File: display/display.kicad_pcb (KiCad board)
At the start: 2 copper layers, 70 x 30 mm, 4 parts, among them J2 Conn_02x05_Odd_Even, U1 D148K, U2 D148K, U3 D148K

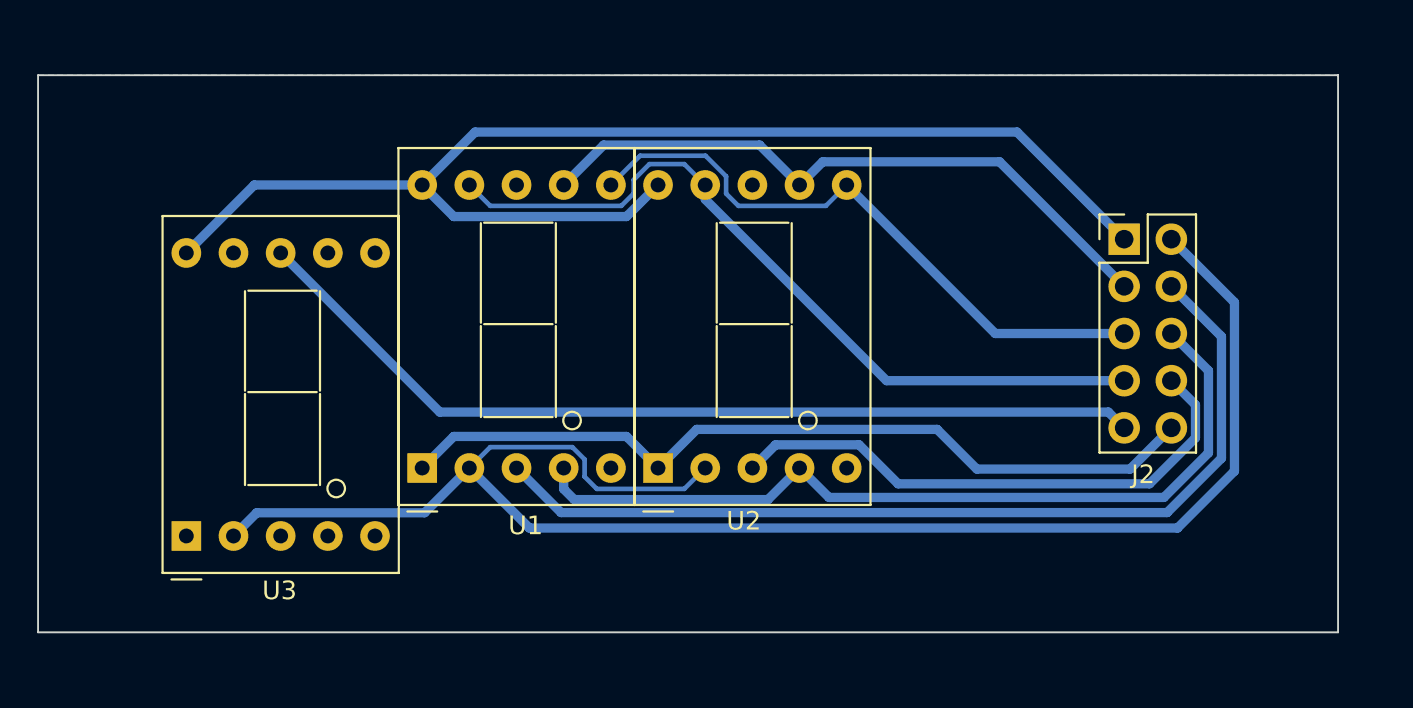
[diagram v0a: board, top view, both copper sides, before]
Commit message: display mod + plano
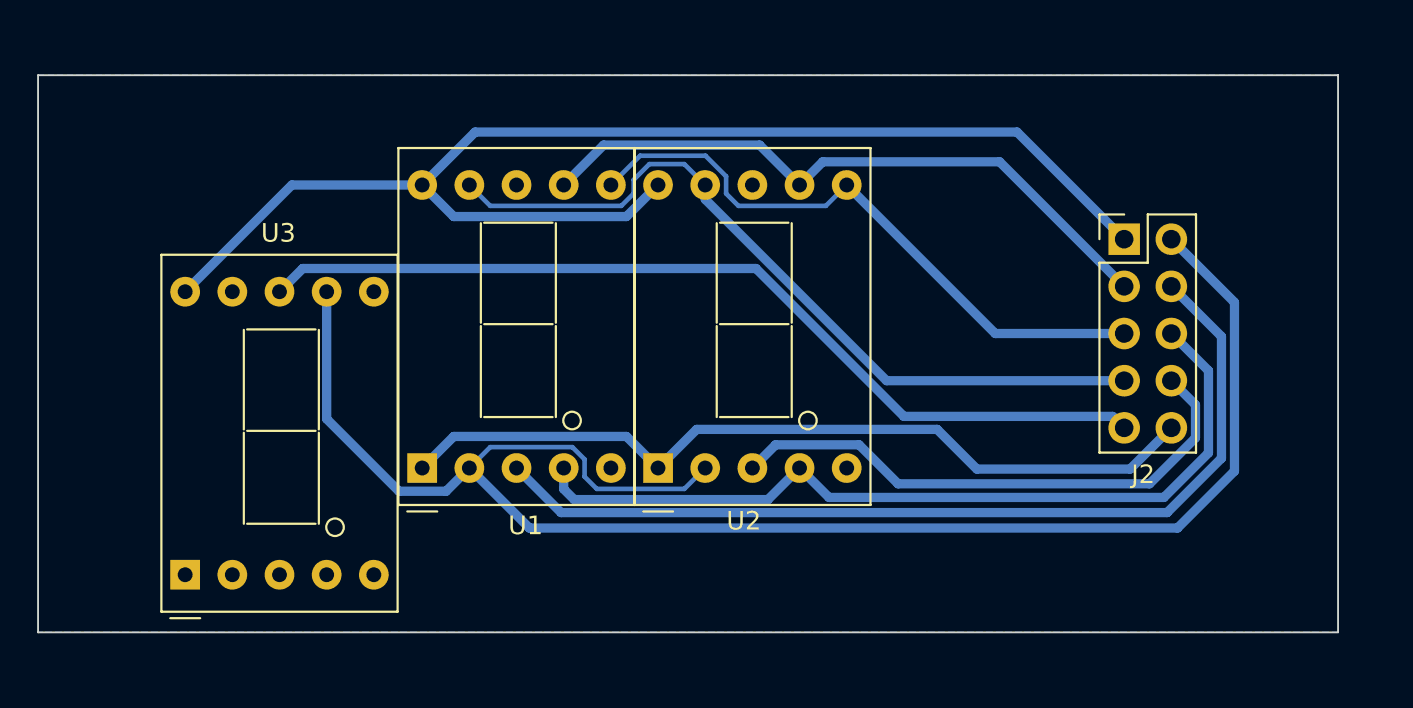
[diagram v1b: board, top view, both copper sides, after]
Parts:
- moved U3 2.09 mm to (57.9, 76.9)
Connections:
- U3 pad 2: /d -> unconnected-(U3-D-Pad2)
- U3 pad 7: unconnected-(U3-A-Pad7) -> /d
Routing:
- net /d: track 87.0 -> 89.5 mm
- net /g: track 69.7 -> 70.6 mm
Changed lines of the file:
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@@
   (net 5 "/cs3")
   (net 6 "unconnected-(U3-F-Pad9)")
-  (net 7 "unconnected-(U3-A-Pad7)")
+  (net 7 "unconnected-(U3-D-Pad2)")
   (net 8 "unconnected-(U3-B-Pad6)")
   (net 9 "unconnected-(U3-C-Pad4)")
@@
   )
   (footprint "Display_7Segment:D1X8K" (layer "F.Cu")
-    (at 57.983 74.811 90)
+    (at 57.92 76.8975 90)
     (descr "https://ia800903.us.archive.org/24/items/CTKD1x8K/Cromatek%20D168K.pdf")
     (tags "Single digit 7 segment ultra bright red")
@@
     (property "ki_keywords" "display LED 7-segment")
     (attr through_hole)
-    (fp_text reference "U3" (at -2.939 5.017 180) (layer "F.SilkS")
+    (fp_text reference "U3" (at 18.3975 5.017 180) (layer "F.SilkS")
         (effects (font (size 1 1) (thickness 0.15)))
     )
@@
       (net 10 "unconnected-(U3-E-Pad1)") (pinfunction "E") (pintype "input+no_connect"))
     (pad "2" thru_hole circle (at 0 2.54) (size 1.6 1.6) (drill 0.8) (layers "*.Cu" "*.Mask")
-      (net 12 "/d") (pinfunction "D") (pintype "input"))
+      (net 7 "unconnected-(U3-D-Pad2)") (pinfunction "D") (pintype "input+no_connect"))
     (pad "3" thru_hole circle (at 0 5.08) (size 1.6 1.6) (drill 0.8) (layers "*.Cu" "*.Mask")
       (net 5 "/cs3") (pinfunction "CC") (pintype "input"))
@@
       (net 8 "unconnected-(U3-B-Pad6)") (pinfunction "B") (pintype "input+no_connect"))
     (pad "7" thru_hole circle (at 15.24 7.62) (size 1.6 1.6) (drill 0.8) (layers "*.Cu" "*.Mask")
-      (net 7 "unconnected-(U3-A-Pad7)") (pinfunction "A") (pintype "input+no_connect"))
+      (net 12 "/d") (pinfunction "A") (pintype "input"))
     (pad "8" thru_hole circle (at 15.24 5.08) (size 1.6 1.6) (drill 0.8) (layers "*.Cu" "*.Mask")
       (net 5 "/cs3") (pinfunction "CC") (pintype "input"))
@@
   (gr_rect (start 50 50) (end 120 80)
     (stroke (width 0.1) (type default)) (fill none) (layer "Edge.Cuts"))
+  (dimension (type orthogonal) (layer "User.1")
+    (pts (xy 50.5 46.9) (xy 58.2 86.9))
+    (height -6.2)
+    (orientation 1)
+    (gr_text "40.0000 mm" (at 43.15 66.9 90) (layer "User.1")
+      (effects (font (size 1 1) (thickness 0.15)))
+    )
+    (format (prefix "") (suffix "") (units 3) (units_format 1) (precision 4))
+    (style (thickness 0.15) (arrow_length 1.27) (text_position_mode 0) (extension_height 0.58642) (extension_offset 0.5) keep_text_aligned)
+  )
+  (dimension (type orthogonal) (layer "User.1")
+    (pts (xy 70.4 53.9) (xy 71.1 46.9))
+    (height -22.9)
+    (orientation 1)
+    (gr_text "7.0000 mm" (at 46.35 50.4 90) (layer "User.1")
+      (effects (font (size 1 1) (thickness 0.15)))
+    )
+    (format (prefix "") (suffix "") (units 3) (units_format 1) (precision 4))
+    (style (thickness 0.15) (arrow_length 1.27) (text_position_mode 0) (extension_height 0.58642) (extension_offset 0.5) keep_text_aligned)
+  )
+  (dimension (type orthogonal) (layer "User.1")
+    (pts (xy 57.5 86.9) (xy 57.5 78.9))
+    (height -1.5)
+    (orientation 1)
+    (gr_text "8.0000 mm" (at 54.85 82.9 90) (layer "User.1")
+      (effects (font (size 1 1) (thickness 0.15)))
+    )
+    (format (prefix "") (suffix "") (units 3) (units_format 1) (precision 4))
+    (style (thickness 0.15) (arrow_length 1.27) (text_position_mode 0) (extension_height 0.58642) (extension_offset 0.5) keep_text_aligned)
+  )
   (segment (start 87.71 57.036) (end 87.048 56.374) (width 0.25) (layer "B.Cu") (net 1))
   (segment (start 101.541 63.909) (end 93.543 55.911) (width 0.5) (layer "B.Cu") (net 1))
@@
   (segment (start 72.383 57.611) (end 81.683 57.611) (width 0.5) (layer "B.Cu") (net 4))
   (segment (start 102.714 53.061) (end 108.482 58.829) (width 0.5) (layer "B.Cu") (net 4))
+  (segment (start 63.6665 55.911) (end 70.683 55.911) (width 0.5) (layer "B.Cu") (net 4))
+  (segment (start 57.92 61.6575) (end 63.6665 55.911) (width 0.5) (layer "B.Cu") (net 4))
   (segment (start 73.533 53.061) (end 102.714 53.061) (width 0.5) (layer "B.Cu") (net 4))
-  (segment (start 61.643 55.911) (end 70.683 55.911) (width 0.5) (layer "B.Cu") (net 4))
   (segment (start 70.683 55.911) (end 73.533 53.061) (width 0.5) (layer "B.Cu") (net 4))
-  (segment (start 57.983 59.571) (end 61.643 55.911) (width 0.5) (layer "B.Cu") (net 4))
   (segment (start 70.683 55.911) (end 72.383 57.611) (width 0.5) (layer "B.Cu") (net 4))
   (segment (start 81.683 57.611) (end 83.383 55.911) (width 0.5) (layer "B.Cu") (net 4))
-  (segment (start 107.632 68.139) (end 71.631 68.139) (width 0.5) (layer "B.Cu") (net 5))
-  (segment (start 71.631 68.139) (end 63.063 59.571) (width 0.5) (layer "B.Cu") (net 5))
-  (segment (start 108.482 68.989) (end 107.632 68.139) (width 0.5) (layer "B.Cu") (net 5))
+  (segment (start 96.620817 68.371) (end 107.864 68.371) (width 0.5) (layer "B.Cu") (net 5))
+  (segment (start 107.864 68.371) (end 108.482 68.989) (width 0.5) (layer "B.Cu") (net 5))
+  (segment (start 63 61.6575) (end 64.25 60.4075) (width 0.5) (layer "B.Cu") (net 5))
+  (segment (start 64.25 60.4075) (end 88.657317 60.4075) (width 0.5) (layer "B.Cu") (net 5))
+  (segment (start 88.657317 60.4075) (end 96.620817 68.371) (width 0.5) (layer "B.Cu") (net 5))
   (segment (start 72.383 69.451) (end 81.683 69.451) (width 0.5) (layer "B.Cu") (net 11))
   (segment (start 108.803 71.208) (end 100.55 71.208) (width 0.5) (layer "B.Cu") (net 11))
@@
   (segment (start 111.022 68.989) (end 108.803 71.208) (width 0.5) (layer "B.Cu") (net 11))
   (segment (start 83.383 71.151) (end 83.383 70.649) (width 0.25) (layer "B.Cu") (net 11))
-  (segment (start 70.813 73.561) (end 73.223 71.151) (width 0.5) (layer "B.Cu") (net 12))
+  (segment (start 65.54 61.6575) (end 65.54 68.508) (width 0.5) (layer "B.Cu") (net 12))
   (segment (start 80.087009 72.276) (end 79.428 71.616991) (width 0.25) (layer "B.Cu") (net 12))
   (segment (start 84.798 72.276) (end 80.087009 72.276) (width 0.25) (layer "B.Cu") (net 12))
@@
   (segment (start 74.348 70.026) (end 73.223 71.151) (width 0.25) (layer "B.Cu") (net 12))
   (segment (start 114.422 71.317) (end 111.356 74.383) (width 0.5) (layer "B.Cu") (net 12))
-  (segment (start 60.523 74.811) (end 61.773 73.561) (width 0.5) (layer "B.Cu") (net 12))
+  (segment (start 71.973 72.401) (end 73.223 71.151) (width 0.5) (layer "B.Cu") (net 12))
+  (segment (start 69.433 72.401) (end 71.973 72.401) (width 0.5) (layer "B.Cu") (net 12))
   (segment (start 111.356 74.383) (end 76.455 74.383) (width 0.5) (layer "B.Cu") (net 12))
   (segment (start 79.428 70.685009) (end 78.768991 70.026) (width 0.25) (layer "B.Cu") (net 12))
@@
   (segment (start 111.022 58.829) (end 114.422 62.229) (width 0.5) (layer "B.Cu") (net 12))
   (segment (start 78.768991 70.026) (end 74.348 70.026) (width 0.25) (layer "B.Cu") (net 12))
-  (segment (start 61.773 73.561) (end 70.813 73.561) (width 0.5) (layer "B.Cu") (net 12))
+  (segment (start 65.54 68.508) (end 69.433 72.401) (width 0.5) (layer "B.Cu") (net 12))
   (segment (start 114.422 62.229) (end 114.422 71.317) (width 0.5) (layer "B.Cu") (net 12))
   (segment (start 113.722 70.62595) (end 110.79695 73.551) (width 0.5) (layer "B.Cu") (net 13))

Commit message: update display pcb
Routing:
- net /d: track 89.5 -> 102.3 mm
- net /g: track 70.6 -> 79.2 mm
- net /cs1: track 50.5 -> 56.9 mm
- net /c: track 45.7 -> 51.9 mm
- net /f: track 42.4 -> 47.9 mm
- net /b: track 33.7 -> 38.7 mm
- net /a: track 35.3 -> 39.8 mm
- net /e: track 44.9 -> 48.8 mm
- net /cs2: track 29.9 -> 33.8 mm
- net /cs3: track 49.6 -> 51.0 mm
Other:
- board size 70 x 30 mm -> 70 x 34 mm

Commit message: mod display
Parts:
- moved U3 1.98 mm to (57.4, 75.0)
- moved U1 0.31 mm to (70.4, 71.2)
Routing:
- net /cs3: track 51.0 -> 67.0 mm
- net /g: track 79.2 -> 75.8 mm
- net /cs2: track 33.8 -> 30.9 mm
- net /b: track 38.7 -> 36.0 mm
- net /f: track 47.9 -> 45.3 mm
- net /c: track 51.9 -> 50.4 mm
- net /d: track 102.3 -> 100.8 mm
- net /cs1: track 56.9 -> 55.6 mm
- net /e: track 48.8 -> 48.0 mm

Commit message: 3 sketch arduino
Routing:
- net /d: track 100.8 -> 120.2 mm
- net /cs1: track 55.6 -> 67.2 mm
- net /c: track 50.4 -> 60.3 mm
- net /g: track 75.8 -> 84.2 mm
- net /cs2: track 30.9 -> 37.6 mm
- net /a: track 39.6 -> 46.2 mm
- net /e: track 48.0 -> 53.5 mm
- net /b: track 36.0 -> 39.3 mm
- net /cs3: track 67.0 -> 67.8 mm
